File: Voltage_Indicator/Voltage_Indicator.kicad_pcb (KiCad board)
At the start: 2 copper layers, 50.9 x 56.9 mm, 27 parts, among them IC1 TLV2371QDBVRQ1, J1 PET-02-XX-X-VT-LC, U1 LM393LVQDDFRQ1, U2 IPBT-102-H1-XX-S-RA, U3 PAMC0381D10QDFXRQ1

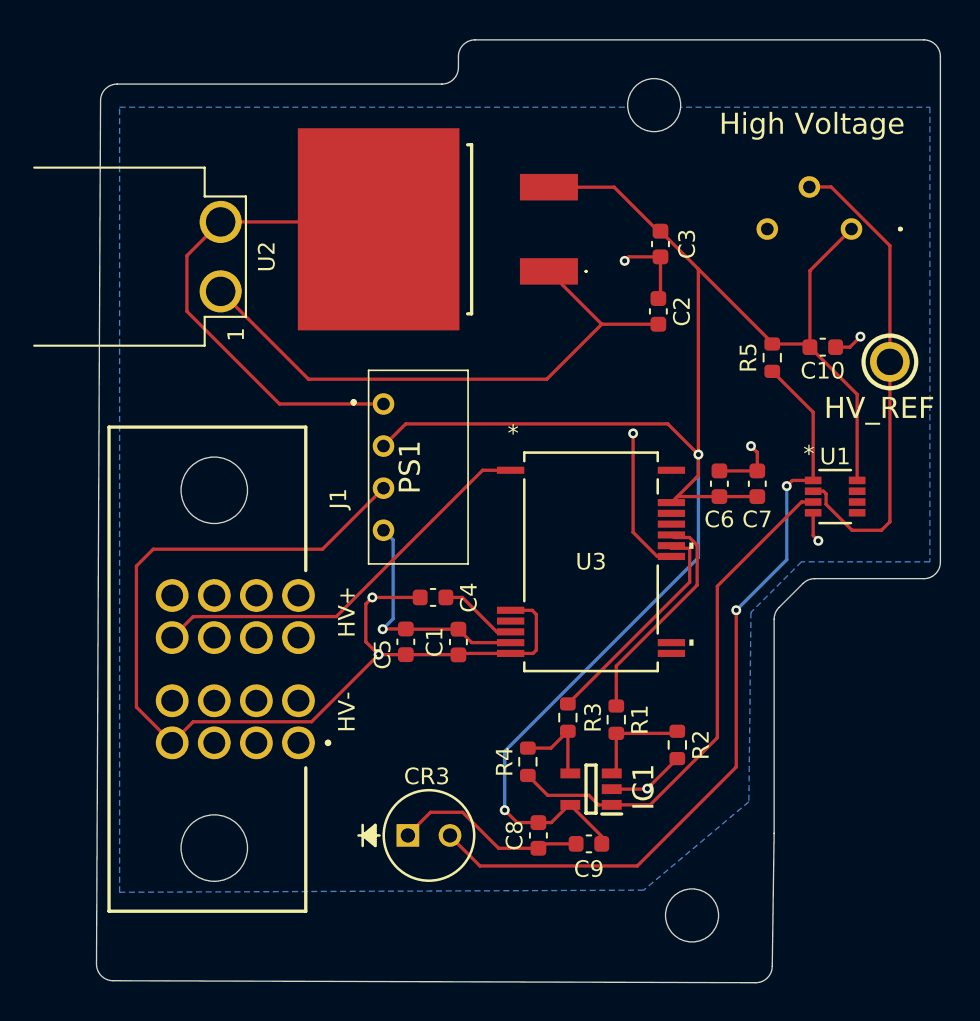
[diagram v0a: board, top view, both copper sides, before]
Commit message: Fixed Voltage Indicator Board Shape
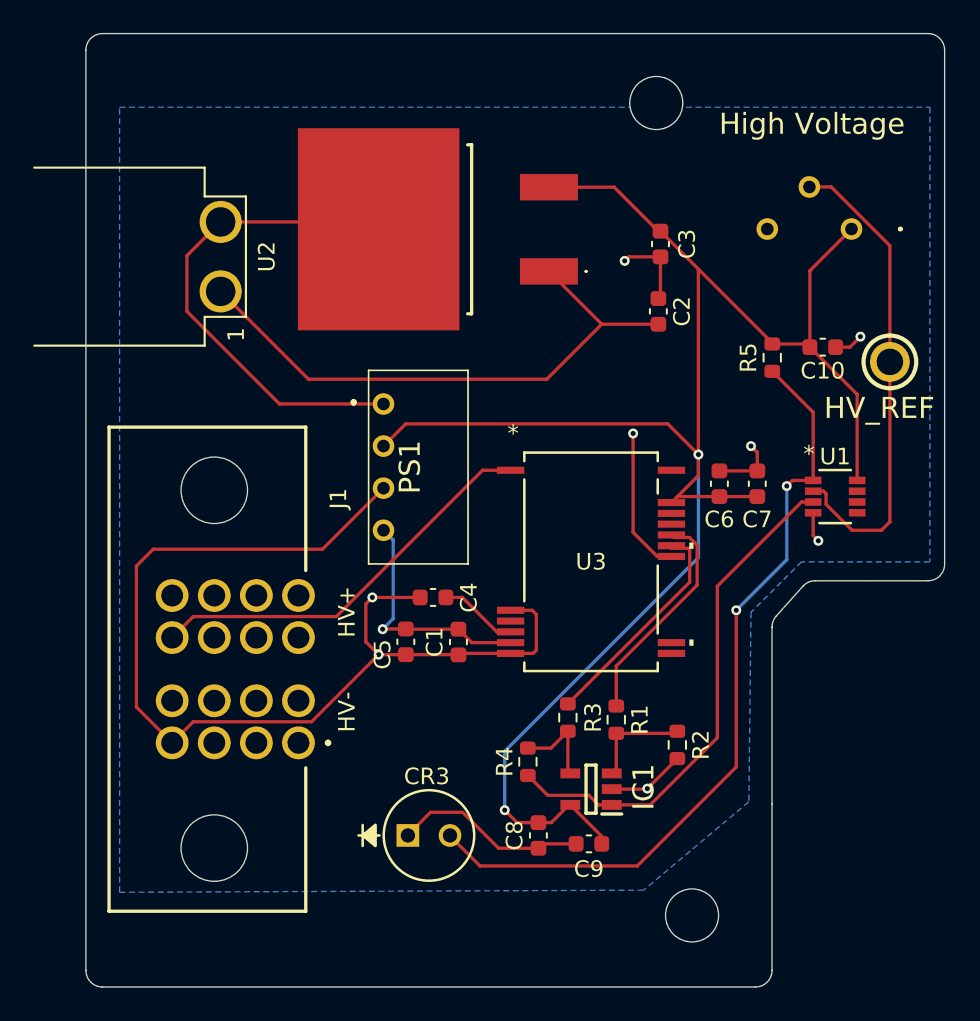
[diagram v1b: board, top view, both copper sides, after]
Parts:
- moved REF** 0.18 mm to (168.8, 65.7)
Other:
- board size 50.9 x 56.9 mm -> 51.8 x 57.5 mm
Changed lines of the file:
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@@
 	(footprint "MountingHole:MountingHole_3.2mm_M3"
 		(layer "F.Cu")
-		(at 168.656 65.786)
+		(at 168.783 65.659)
 		(descr "Mounting Hole 3.2mm, M3, no annular, generated by kicad-footprint-generator mountinghole.py")
 		(tags "mountinghole M3")
@@
 		(embedded_fonts no)
 	)
-	(gr_line
-		(start 155.845 64.516)
-		(end 136.250316 64.516)
-		(stroke
-			(width 0.05)
-			(type default)
-		)
-		(layer "Edge.Cuts")
-	)
-	(gr_arc
-		(start 156.845 63.516)
-		(mid 156.552107 64.223107)
-		(end 155.845 64.516)
-		(stroke
-			(width 0.05)
-			(type default)
-		)
-		(layer "Edge.Cuts")
-	)
 	(gr_arc
-		(start 175.895 109.720958)
-		(mid 175.894975 109.728)
-		(end 175.894901 109.735041)
+		(start 134.366 62.468)
+		(mid 134.658893 61.760893)
+		(end 135.366 61.468)
 		(stroke
 			(width 0.05)
@@
 	)
 	(gr_line
-		(start 178.341214 94.361)
-		(end 184.928 94.361)
+		(start 134.366 117.999)
+		(end 134.366 62.468)
 		(stroke
 			(width 0.05)
@@
 	)
 	(gr_line
-		(start 185.928 93.361)
-		(end 185.928 62.849)
+		(start 135.366 61.468)
+		(end 168.91 61.468)
 		(stroke
 			(width 0.05)
@@
 		(layer "Edge.Cuts")
 	)
-	(gr_line
-		(start 176.187893 96.100107)
-		(end 177.634107 94.653893)
+	(gr_arc
+		(start 135.366 118.999)
+		(mid 134.658893 118.706107)
+		(end 134.366 117.999)
 		(stroke
 			(width 0.05)
@@
 		(layer "Edge.Cuts")
 	)
-	(gr_arc
-		(start 156.845 62.849)
-		(mid 157.137893 62.141893)
-		(end 157.845 61.849)
+	(gr_line
+		(start 168.91 61.468)
+		(end 185.182 61.468)
 		(stroke
 			(width 0.05)
@@
 		(layer "Edge.Cuts")
 	)
-	(gr_arc
-		(start 136.002576 118.62112)
-		(mid 135.295828 118.325465)
-		(end 135.005702 117.61643)
+	(gr_line
+		(start 174.768 118.999)
+		(end 135.366 118.999)
 		(stroke
 			(width 0.05)
@@
 		(layer "Edge.Cuts")
 	)
-	(gr_arc
-		(start 175.781929 117.756007)
-		(mid 175.483022 118.45508)
-		(end 174.778914 118.741919)
+	(gr_line
+		(start 175.768 97.283065)
+		(end 175.768 107.95)
 		(stroke
 			(width 0.05)
@@
 	)
 	(gr_arc
-		(start 177.634107 94.653893)
-		(mid 177.95853 94.43712)
-		(end 178.341214 94.361)
+		(start 175.768 97.283065)
+		(mid 175.833869 96.926169)
+		(end 176.022758 96.61627)
 		(stroke
 			(width 0.05)
@@
 	)
 	(gr_line
-		(start 156.845 62.849)
-		(end 156.845 63.516)
+		(start 175.768 107.95)
+		(end 175.768 117.999)
 		(stroke
 			(width 0.05)
@@
 	)
 	(gr_arc
-		(start 184.928 61.849)
-		(mid 185.635107 62.141893)
-		(end 185.928 62.849)
-		(stroke
-			(width 0.05)
-			(type default)
-		)
-		(layer "Edge.Cuts")
-	)
-	(gr_line
-		(start 175.781929 117.756007)
-		(end 175.894901 109.735041)
+		(start 175.768 117.999)
+		(mid 175.475107 118.706107)
+		(end 174.768 118.999)
 		(stroke
 			(width 0.05)
@@
 	)
 	(gr_line
-		(start 135.250327 65.511305)
-		(end 135.005702 117.61643)
+		(start 177.628869 94.821205)
+		(end 176.022758 96.61627)
 		(stroke
 			(width 0.05)
@@
 		(layer "Edge.Cuts")
 	)
-	(gr_line
-		(start 175.895 109.720958)
-		(end 175.895 96.807214)
+	(gr_arc
+		(start 177.628869 94.821205)
+		(mid 177.96594 94.575094)
+		(end 178.37411 94.488)
 		(stroke
 			(width 0.05)
@@
 	)
 	(gr_arc
-		(start 175.895 96.807214)
-		(mid 175.97112 96.424531)
-		(end 176.187893 96.100107)
+		(start 185.182 61.468)
+		(mid 185.889107 61.760893)
+		(end 186.182 62.468)
 		(stroke
 			(width 0.05)
@@
 	)
 	(gr_line
-		(start 136.002576 118.62112)
-		(end 174.778914 118.741919)
+		(start 185.182 94.488)
+		(end 178.37411 94.488)
 		(stroke
 			(width 0.05)
@@
 		(layer "Edge.Cuts")
 	)
-	(gr_arc
-		(start 135.250327 65.511305)
-		(mid 135.544871 64.807235)
-		(end 136.250316 64.516)
+	(gr_line
+		(start 186.182 62.468)
+		(end 186.182 93.488)
 		(stroke
 			(width 0.05)
@@
 	)
 	(gr_arc
-		(start 185.928 93.361)
-		(mid 185.635107 94.068107)
-		(end 184.928 94.361)
-		(stroke
-			(width 0.05)
-			(type default)
-		)
-		(layer "Edge.Cuts")
-	)
-	(gr_line
-		(start 184.928 61.849)
-		(end 157.845 61.849)
+		(start 186.182 93.488)
+		(mid 185.889107 94.195107)
+		(end 185.182 94.488)
 		(stroke
 			(width 0.05)
@@
 		(layer "Edge.Cuts")
 	)
-	(gr_text "HV-"
-		(at 150.704 103.639 90)
+	(gr_text "HV+"
+		(at 150.704 97.924 90)
 		(layer "F.SilkS")
 		(effects
@@
 		)
 	)
-	(gr_text "HV+"
-		(at 150.704 97.924 90)
+	(gr_text "HV-"
+		(at 150.704 103.639 90)
 		(layer "F.SilkS")
 		(effects
